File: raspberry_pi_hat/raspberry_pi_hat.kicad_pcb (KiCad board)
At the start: 2 copper layers, 91.9 x 80.6 mm, 19 parts, among them IC2 LD1117v33, J1 LCD_screeen, J3 GPIO, J4 GPIO, J5 Switches, J6 LED_status, J7 Screw_Terminal_01x02, U1 NRF24L01P

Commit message: Completed redistribution of boards
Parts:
- J1: footprint Connector_Molex:Molex_KK-396_A-41792-0004_1x04_P3.96mm_Horizontal -> Connector_Molex:Molex_KK-254_AE-6410-04A_1x04_P2.54mm_Vertical
- moved C3 25.3 mm to (157.0, 147.0), turned to 135 degrees
- moved IC2 23.5 mm to (162.0, 144.9), turned to -90 degrees
- moved C4 22.9 mm to (151.5, 148.0), turned to 135 degrees
- moved U1 19.6 mm to (145.8, 137.5)
- moved J7 19.5 mm to (170.7, 127.0)
- moved C2 18.1 mm to (170.6, 146.0), turned to 145 degrees
- moved C1 16.5 mm to (172.2, 139.5), turned to 180 degrees
- moved J1 4.13 mm to (94.8, 187.3)
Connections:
- J3 pad 15: /Transceiver/GPIO22 -> CE
- J3 pad 22: CE -> /Transceiver/GPIO25
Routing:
- net CE: track 97.2 -> 44.3 mm, vias 0 -> 2
- net GND: track 305.4 -> 275.1 mm
- net CSN: track 107.0 -> 81.8 mm, vias 2 -> 1
- net +5V: track 124.7 -> 139.3 mm
- net +3V3: track 37.1 -> 25.4 mm
- net /Transceiver/GPIO11/SPI0.SCLK: track 13.7 -> 25.2 mm
- net /Transceiver/GPIO9/SPI0.MISO: track 9.82 -> 20.6 mm
- net /Transceiver/GPIO10/SPI0.MOSI: track 16.4 -> 22.4 mm
- net /interface/GPIO3/SCL1: track 22.9 -> 21.2 mm
- net /interface/GPIO2/SDA1: track 18.4 -> 17.2 mm

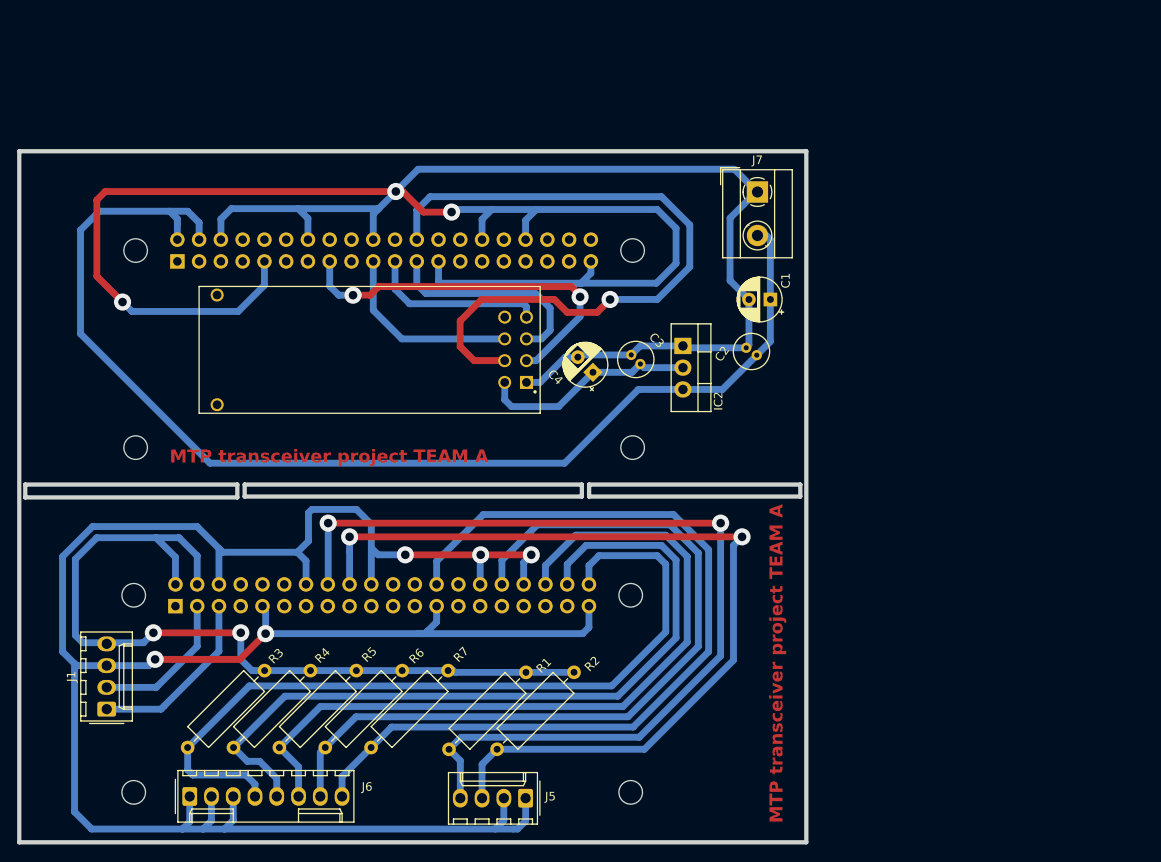
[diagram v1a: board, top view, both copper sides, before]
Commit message: Combined both PCBs successfully and solved errors
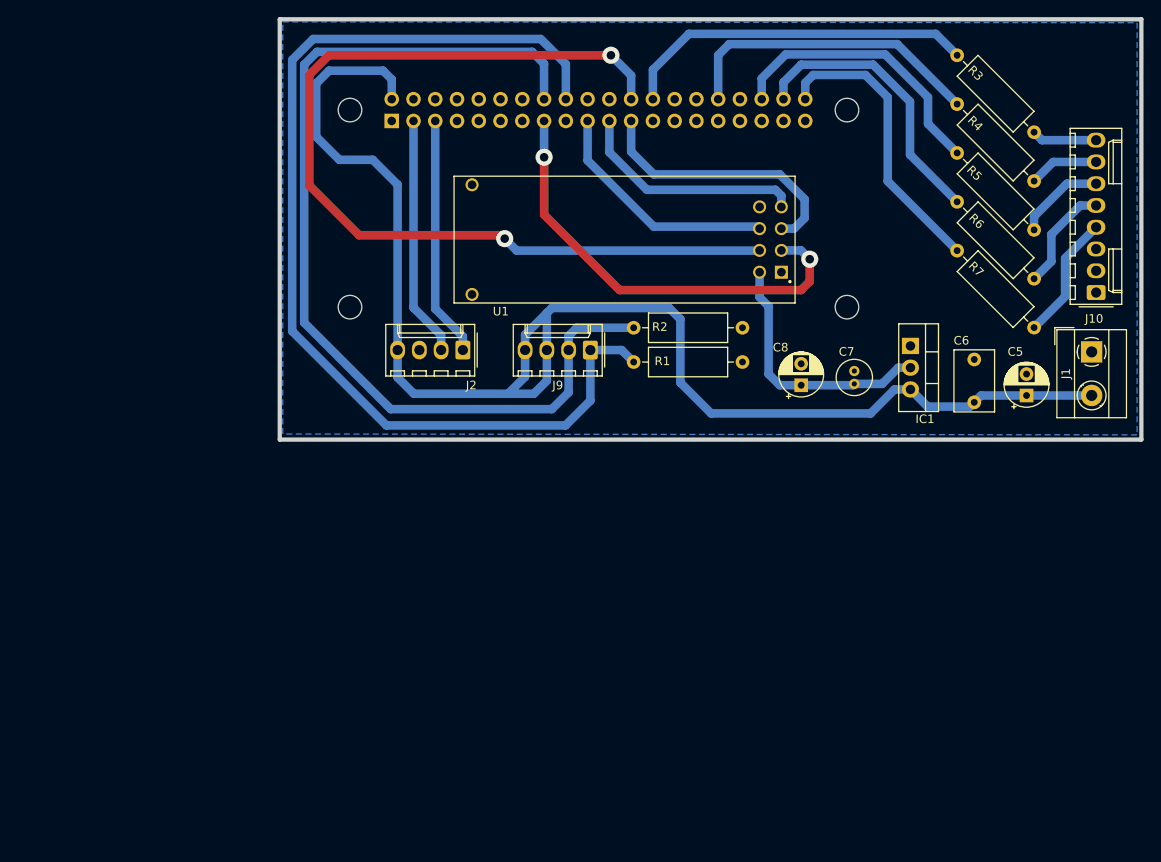
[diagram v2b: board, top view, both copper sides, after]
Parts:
- removed C1, C4: 10uF, Capacitor_THT:CP_Radial_D5.0mm_P2.50mm
- removed C2: 0,47uF, Capacitor_THT:C_Radial_D4.0mm_H5.0mm_P1.50mm
- removed C3: 33uF, Capacitor_THT:C_Radial_D4.0mm_H5.0mm_P1.50mm
- removed IC2: LD1117v33, Package_TO_SOT_THT:TO-220-3_Vertical
- removed J3, J4: GPIO, Module:Raspberry_Pi_Zero_Socketed_THT_FaceDown_MountingHoles
- removed J5: Switches, Connector_Molex:Molex_KK-254_AE-6410-04A_1x04_P2.54mm_Vertical
- removed J6: LED_status, Connector_Molex:Molex_KK-254_AE-6410-08A_1x08_P2.54mm_Vertical
- removed J7: Screw_Terminal_01x02, TerminalBlock_MetzConnect:TerminalBlock_MetzConnect_Type101_RT01602HBWC_1x02_P5.08mm_Horizontal
- added C5: 10uF, Capacitor_THT:CP_Radial_D5.0mm_P2.50mm, F.Cu at (202.1, 150.7)
- added C6: 0,47uF, Capacitor_THT:C_Rect_L7.0mm_W4.5mm_P5.00mm, F.Cu at (196.0, 151.5)
- added C7: 33uF, Capacitor_THT:C_Radial_D4.0mm_H5.0mm_P1.50mm, F.Cu at (182.0, 149.3)
- added C8: 10uF, Capacitor_THT:CP_Radial_D5.0mm_P2.50mm, F.Cu at (175.8, 149.5)
- added IC1: LD1117v33, Package_TO_SOT_THT:TO-220-3_Vertical, F.Cu at (188.6, 144.9)
- added J10: LED_status, Connector_Molex:Molex_KK-254_AE-6410-08A_1x08_P2.54mm_Vertical, F.Cu at (210.2, 138.7)
- added J2: LCD_screeen, Connector_Molex:Molex_KK-254_AE-6410-04A_1x04_P2.54mm_Vertical, F.Cu at (136.3, 145.4)
- added J8: GPIO, Module:Raspberry_Pi_Zero_Socketed_THT_FaceDown_MountingHoles, B.Cu at (130.6, 128.7)
- added J9: Switches, Connector_Molex:Molex_KK-254_AE-6410-04A_1x04_P2.54mm_Vertical, F.Cu at (151.2, 145.4)
- J1: value LCD_screeen -> Screw_Terminal_01x02; footprint Connector_Molex:Molex_KK-254_AE-6410-04A_1x04_P2.54mm_Vertical -> TerminalBlock_MetzConnect:TerminalBlock_MetzConnect_Type101_RT01602HBWC_1x02_P5.08mm_Horizontal
- R1, R2: value 220 -> 10k
- moved J1 122.3 mm to (209.7, 145.6), turned to -90 degrees
- moved R3 108.1 mm to (194.0, 111.0), turned to -45 degrees
- moved R4 100.3 mm to (194.0, 116.7), turned to -45 degrees
- moved R5 92.5 mm to (194.0, 122.4), turned to -45 degrees
- moved R6 84.8 mm to (194.0, 128.1), turned to -45 degrees
- moved R7 77.0 mm to (194.0, 133.8), turned to -45 degrees
- moved R2 40.8 mm to (156.2, 142.8), turned to 0 degrees
- moved R1 38.3 mm to (156.2, 146.8), turned to 0 degrees
- moved U1 32.4 mm to (175.6, 124.6)
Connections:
- J1 pad 1: /interface/GPIO3/SCL1 -> GND
- J1 pad 2: /interface/GPIO2/SDA1 -> +5V
- R1 pad 1: +5VA -> /GPIO24
- R1 pad 2: /interface/GPIO23 -> GND
- R2 pad 1: +5VA -> /GPIO23
- R2 pad 2: /interface/GPIO24 -> GND
- R3 pad 1: +5VA -> /GPIO7/SPI0.CE1
- R3 pad 2: /interface/GPIO21/PCM.DOUT -> Net-(J10-Pin_8)
- R4 pad 1: +5VA -> /GPIO12/PWM0
- R4 pad 2: /interface/GPIO20/PCM.DIN -> Net-(J10-Pin_7)
- R5 pad 1: +5VA -> /GPIO16
- R5 pad 2: /interface/GPIO16 -> Net-(J10-Pin_6)
- R6 pad 1: +5VA -> /GPIO20/PCM.DIN
- R6 pad 2: /interface/GPIO12/PWM0 -> Net-(J10-Pin_5)
- R7 pad 1: +5VA -> /GPIO21/PCM.DOUT
- R7 pad 2: /interface/GPIO7/SPI0.CE1 -> Net-(J10-Pin_4)
- U1 pad 5: /Transceiver/GPIO11/SPI0.SCLK -> /GPIO11/SPI0.SCLK
- U1 pad 6: /Transceiver/GPIO10/SPI0.MOSI -> /GPIO10/SPI0.MOSI
- U1 pad 7: /Transceiver/GPIO9/SPI0.MISO -> /GPIO9/SPI0.MISO
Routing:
- net GND: track 275.1 -> 0.00 mm, vias 3 -> 0
- net GND1: track 261.0 -> 0.00 mm, vias 5 -> 0
- net /GPIO24: track 0.00 -> 122.0 mm
- net /GPIO23: track 0.00 -> 113.9 mm
- net /interface/GPIO23: track 110.2 -> 0.00 mm, vias 2 -> 0
- net /interface/GPIO24: track 104.5 -> 0.00 mm, vias 2 -> 0
- net /interface/GPIO7/SPI0.CE1: track 101.4 -> 0.00 mm
- net +5VA: track 97.5 -> 0.00 mm, vias 2 -> 0
- net /interface/GPIO12/PWM0: track 94.1 -> 0.00 mm
- net /interface/GPIO21/PCM.DOUT: track 93.9 -> 0.00 mm
- net /interface/GPIO20/PCM.DIN: track 91.4 -> 0.00 mm
- net /interface/GPIO16: track 90.6 -> 0.00 mm
- net /GPIO7/SPI0.CE1: track 0.00 -> 41.7 mm
- net /GPIO12/PWM0: track 0.00 -> 36.6 mm
- net /GPIO21/PCM.DOUT: track 0.00 -> 34.2 mm
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- added copper zone on B.Cu, net GND
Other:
- board size 91.9 x 80.6 mm -> 100.5 x 49 mm
- board text removed: "MTP transceiver project TEAM A"

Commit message: improved final version
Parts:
- C6: footprint Capacitor_THT:C_Rect_L7.0mm_W4.5mm_P5.00mm -> Capacitor_THT:C_Radial_D4.0mm_H5.0mm_P1.50mm
- R1, R2: moved to B.Cu
- moved J10 28.7 mm to (205.5, 110.4), turned to -90 degrees
- moved R3 21.9 mm to (186.4, 131.5), turned to 0 degrees
- moved R7 19.8 mm to (186.4, 115.5), turned to 0 degrees
- moved IC1 18.4 mm to (170.2, 145.4)
- moved C7 17.9 mm to (164.2, 149.9), turned to 180 degrees
- moved C6 17.5 mm to (178.5, 151.3)
- moved C5 16.3 mm to (185.8, 151.0)
- moved J1 15.1 mm to (194.6, 145.3)
- moved R4 13.2 mm to (186.4, 127.4), turned to 0 degrees
- moved C8 13.1 mm to (164.0, 143.9), turned to 180 degrees
- moved R6 11.5 mm to (186.4, 119.5), turned to 0 degrees
- moved J9 8.54 mm to (145.0, 151.3), turned to 90 degrees
- moved R2 7.85 mm to (151.5, 149.1), turned to 90 degrees
- moved R5 7.73 mm to (186.4, 123.5), turned to 0 degrees
- moved R1 4.57 mm to (155.8, 151.3), turned to 90 degrees
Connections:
- U1 pad 8: unconnected-(U1-~{IRQ}-Pad8) -> /GPIO27
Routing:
- net GND: track 0.00 -> 83.9 mm, vias 0 -> 7
- net /GPIO27: track 0.00 -> 37.1 mm, vias 0 -> 2
- net /GPIO7/SPI0.CE1: track 41.7 -> 63.8 mm
- net /GPIO21/PCM.DOUT: track 34.2 -> 13.1 mm
- net +5V: track 166.5 -> 146.7 mm
- net /GPIO12/PWM0: track 36.6 -> 49.6 mm
- net /GPIO23: track 113.9 -> 102.9 mm
- net /GPIO20/PCM.DIN: track 33.3 -> 24.7 mm
- net Net-(J10-Pin_4): track 14.7 -> 7.50 mm
- net /GPIO24: track 122.0 -> 114.8 mm
- net Net-(J10-Pin_5): track 12.6 -> 6.91 mm
- net +3V3: track 30.3 -> 25.6 mm
- net Net-(J10-Pin_6): track 10.4 -> 6.62 mm
- net /GPIO16: track 33.0 -> 34.7 mm
- net CSN: track 110.9 -> 111.9 mm
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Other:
- board size 100.5 x 49 mm -> 96.3 x 49.5 mm
- board text added: "MTP Project TEAM A"
